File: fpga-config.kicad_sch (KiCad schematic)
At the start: 21 parts, among them J1 PinHeader_2x7_P2mm_SMD_Shroud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, Q1 BSS138PW, Q2 BSS138PW, Q3 BSS138PW, SW1 CVS-03B, SW2 SW_KMR211NGLFS_SMD, U2 TPD4E05U06QDQARQ1, U4 XC7K160T-FFG676

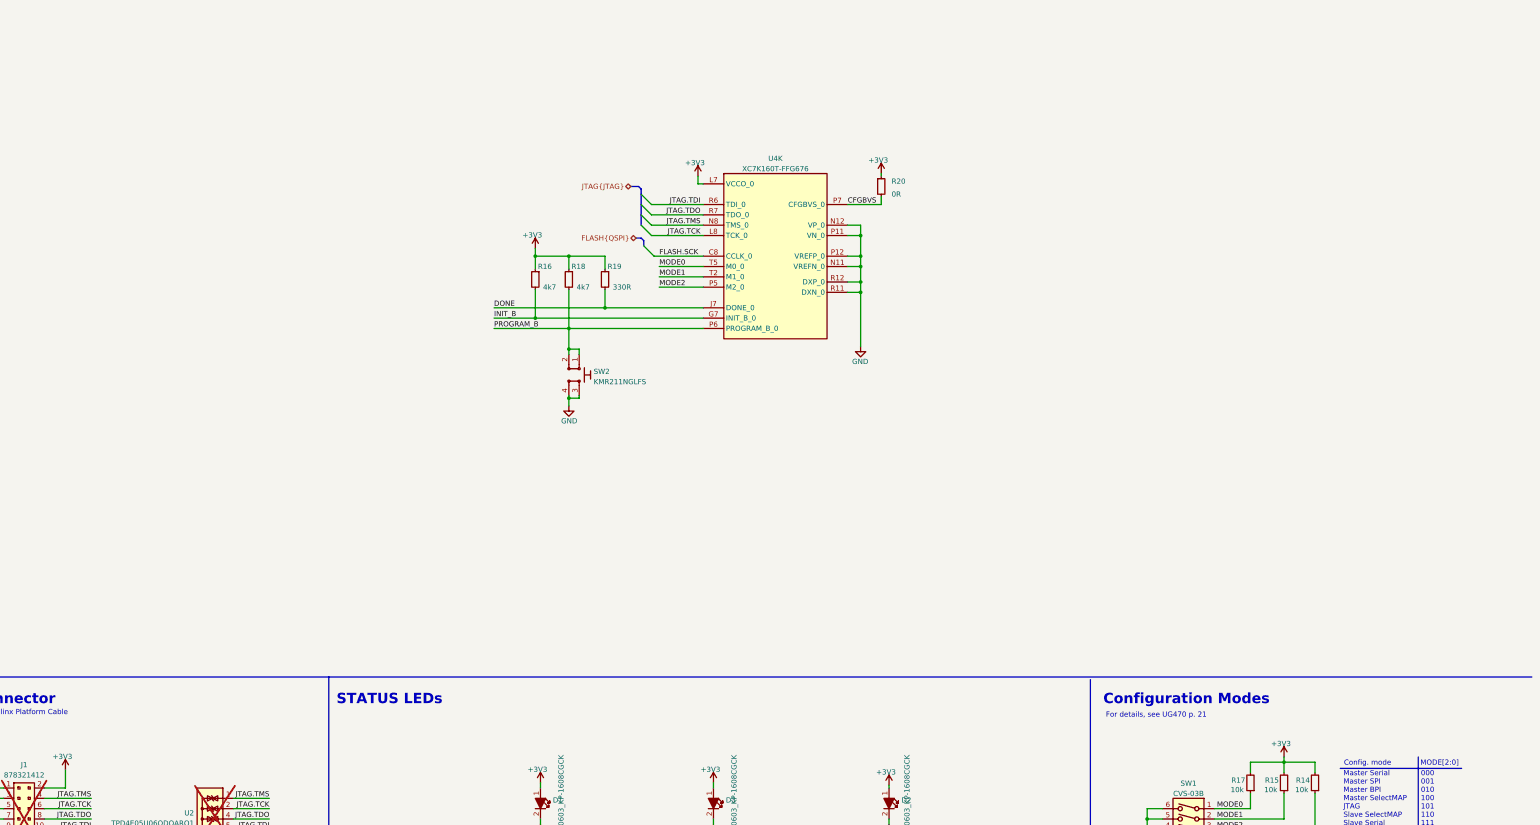
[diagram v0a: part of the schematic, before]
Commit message: [#66311] Add XCAU25P. Reconnect configuration bank 0
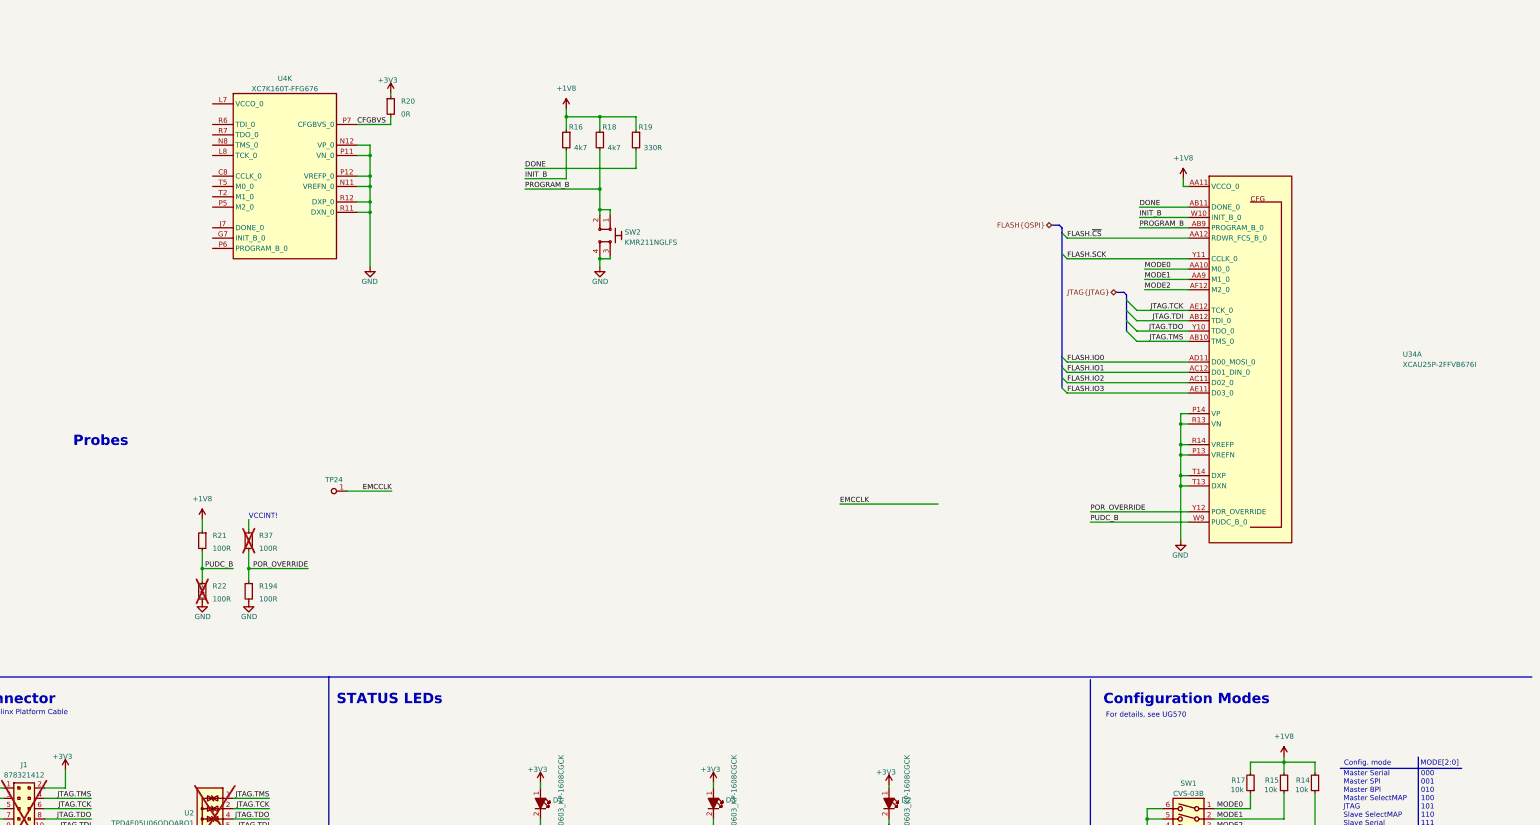
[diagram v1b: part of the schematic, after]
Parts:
- added R194, R21, R22, R37: R_100R_0402, antmicro-footprints:R_0402_1005Metric, symbol antmicroResistors0402:R_100R_0402
- added TP24: TP_1mm_SMD, antmicro-footprints:TP_SMD_1mm, symbol antmicroTestPoints:TP_1mm_SMD
- added U34: XCAU25P-2FFVB676I, antmicro-footprints:BGA-676_27x27mm_Layout26x26_P1x1mm_FFVB676, symbol antmicroFPGAChips:XCAU25P-2FFVB676I
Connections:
- net +3V3: no longer R14.2, R15.2, R16.1, R17.2, R18.1, R19.1, U4.L7 (VCCO_0), U4.T6 (VCCO_0)
- net DONE: now also U34.AB11 (DONE_0); no longer U4.J7 (DONE_0)
- net FLASH.SCK: now also U34.Y11 (CCLK_0); no longer U4.C8 (CCLK_0)
- net GND: now also R194.2, R22.2, U34.P13 (VREFN), U34.P14 (VP), U34.R13 (VN), U34.R14 (VREFP), U34.T13 (DXN), U34.T14 (DXP)
- net INIT_B: now also U34.W10 (INIT_B_0); no longer U4.G7 (INIT_B_0)
- net JTAG.TCK: now also U34.AE12 (TCK_0); no longer U4.L8 (TCK_0)
- net JTAG.TDI: now also U34.AB12 (TDI_0); no longer U4.R6 (TDI_0)
- net JTAG.TDO: now also U34.Y10 (TDO_0); no longer U4.R7 (TDO_0)
- net JTAG.TMS: now also U34.AB10 (TMS_0); no longer U4.N8 (TMS_0)
- net MODE0: now also U34.AA10 (M0_0); no longer U4.T5 (M0_0)
- net MODE1: now also U34.AA9 (M1_0); no longer U4.T2 (M1_0)
- net MODE2: now also U34.AF12 (M2_0); no longer U4.P5 (M2_0)
- net PROGRAM_B: now also U34.AB9 (PROGRAM_B_0); no longer U4.P6 (PROGRAM_B_0)
- new net: U4.L7 (VCCO_0), U4.T6 (VCCO_0)
- new net +1V8: R14.2, R15.2, R16.1, R17.2, R18.1, R19.1, R21.1, U34.AA11 (VCCO_0), U34.AD12 (VCCO_0)
- new net EMCCLK: TP24.1
- new net FLASH.IO0: U34.AD11 (D00_MOSI_0)
- new net FLASH.IO1: U34.AC12 (D01_DIN_0)
- new net FLASH.IO2: U34.AC11 (D02_0)
- new net FLASH.IO3: U34.AE11 (D03_0)
- new net FLASH.~{CS}: U34.AA12 (RDWR_FCS_B_0)
- new net POR_OVERRIDE: R194.1, R37.2, U34.Y12 (POR_OVERRIDE)
- new net PUDC_B: R21.2, R22.1, U34.W9 (PUDC_B_0)
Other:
- note added: "For details, see UG570"
- note added: "Probes"
- note added: "VCCINT!"
- note removed: "For details, see UG470 p. 21"
- moved on the sheet: R16, R18, R19, R20, SW2, U4K

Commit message: [#65754] Rename project
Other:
- title: SO-DIMM DDR5 Tester -> RDIMM DDR5 Tester

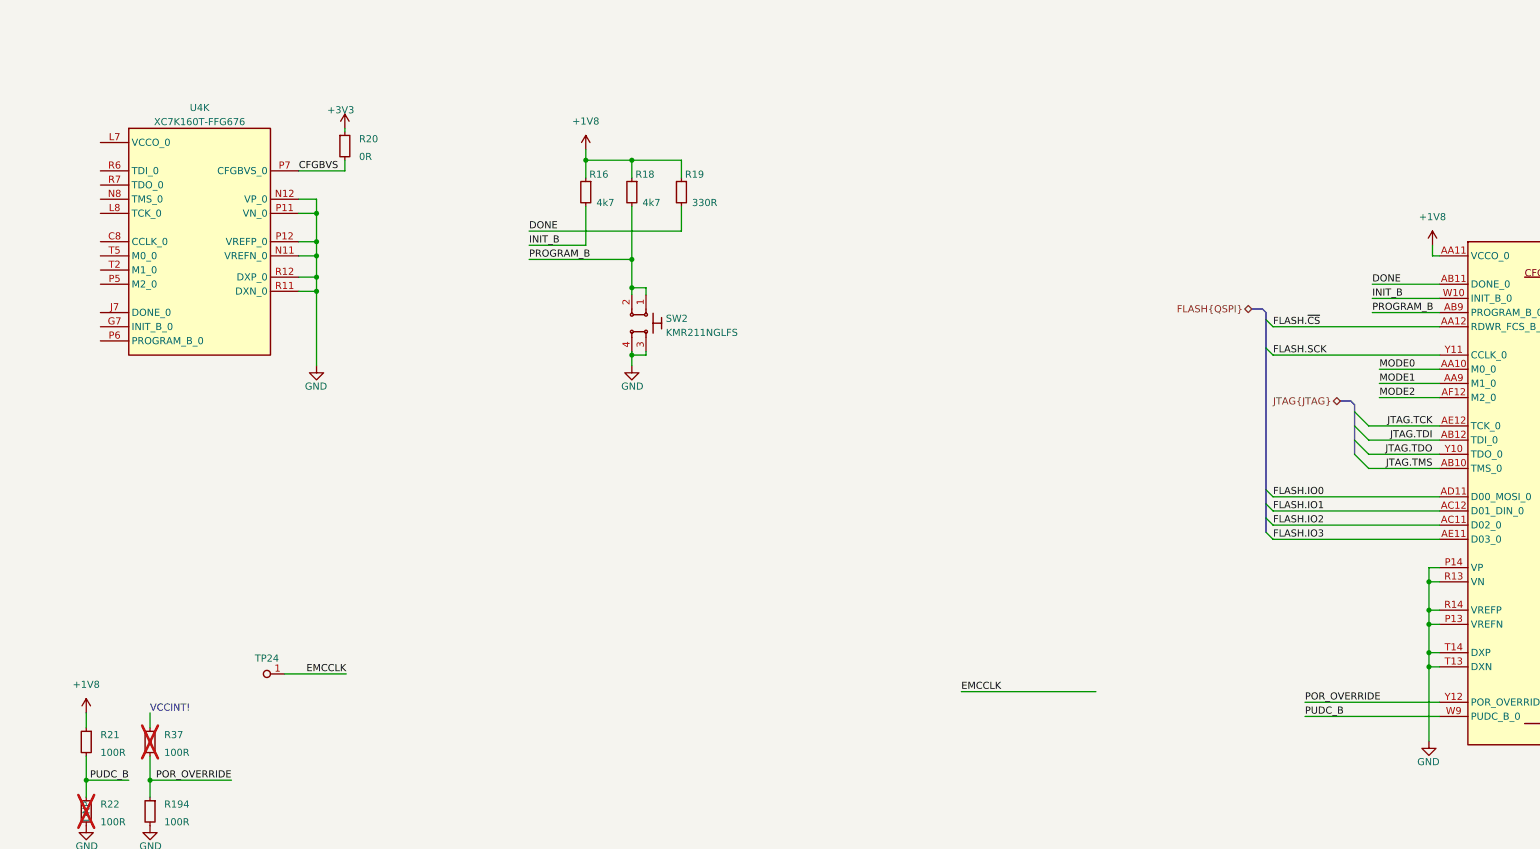
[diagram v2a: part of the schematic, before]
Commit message: [#66311] Add TMP451 remote temperature sensor
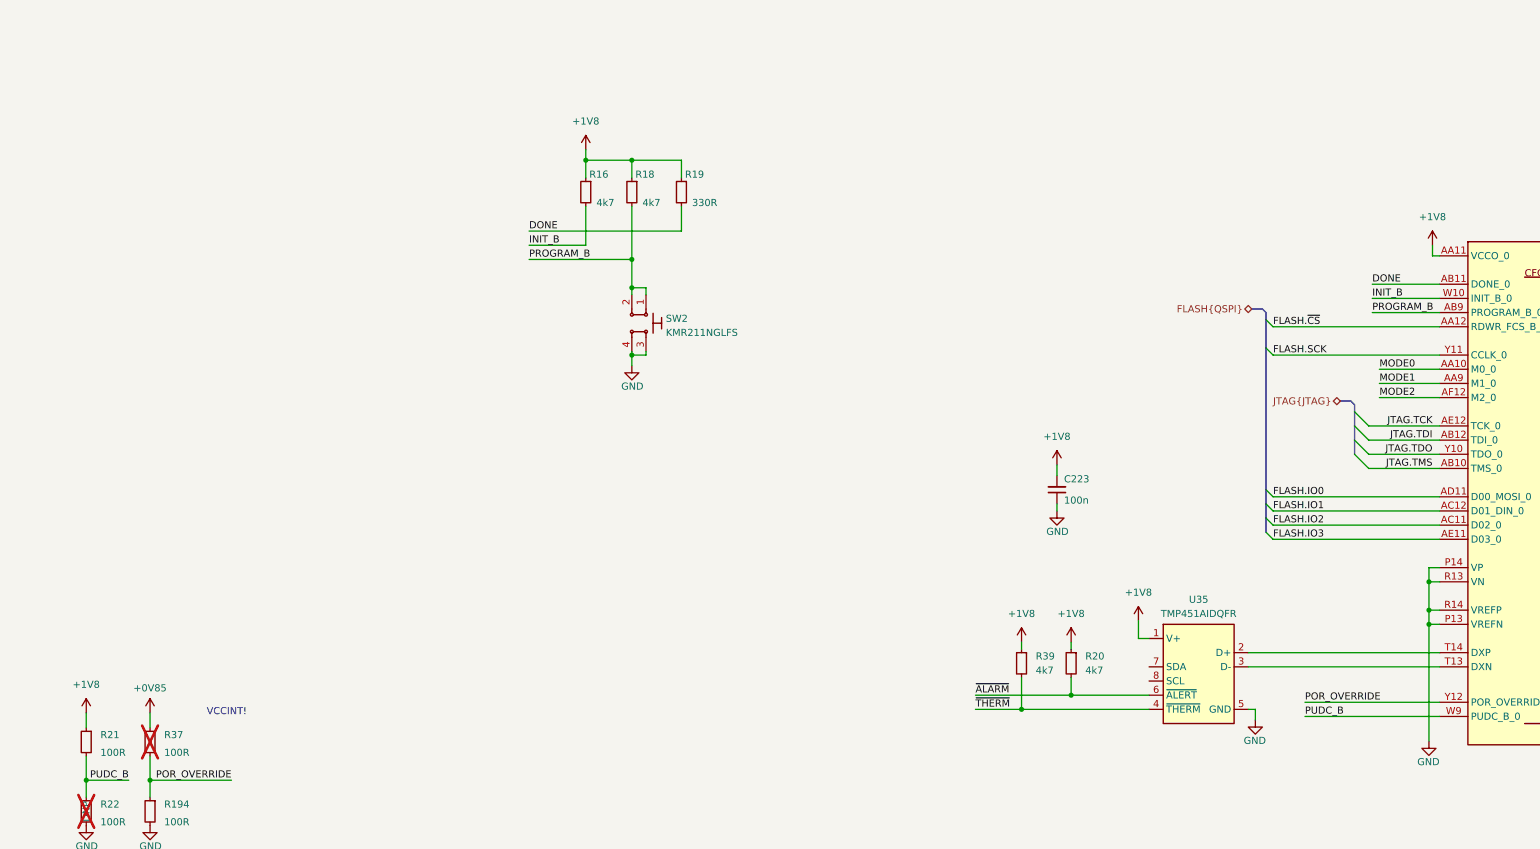
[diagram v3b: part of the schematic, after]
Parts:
- removed R20: R_0R_0402, antmicro-footprints:R_0402_1005Metric, symbol antmicroResistors0402:R_0R_0402
- removed TP24: TP_1mm_SMD, antmicro-footprints:TP_SMD_1mm, symbol antmicroTestPoints:TP_1mm_SMD
- removed U4: XC7K160T-FFG676, antmicro-footprints:BGA-676_27x27mm_Layout26x26_P1x1mm_FFG676, symbol antmicroFPGAChips:XC7K160T-FFG676
- added C223: C_100n_0402, antmicro-footprints:C_0402_1005Metric, symbol antmicroCapacitors0402:C_100n_0402
- added R20, R39: R_4k7_0402, antmicro-footprints:R_0402_1005Metric, symbol antmicroResistors0402:R_4k7_0402
- added U35: TMP451AIDQFR, antmicro-footprints:WSON-8_2x2mm, symbol antmicroTemperatureSensorsAnalogandDigitalOutput:TMP451AIDQFR
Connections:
- net +1V8: now also C223.2, R20.1, R39.1, U35.1 (V+)
- net GND: now also C223.1, U35.5 (GND); no longer U34.T13 (DXN), U34.T14 (DXP)
- net +0V85: now reaches R37.1
- new net: U34.T14 (DXP), U35.2 (D+)
- new net: U34.T13 (DXN), U35.3 (D-)
- new net ~{ALARM}: R20.2, U35.6 (~{ALERT})
- new net ~{THERM}: R39.2, U35.4 (~{THERM})

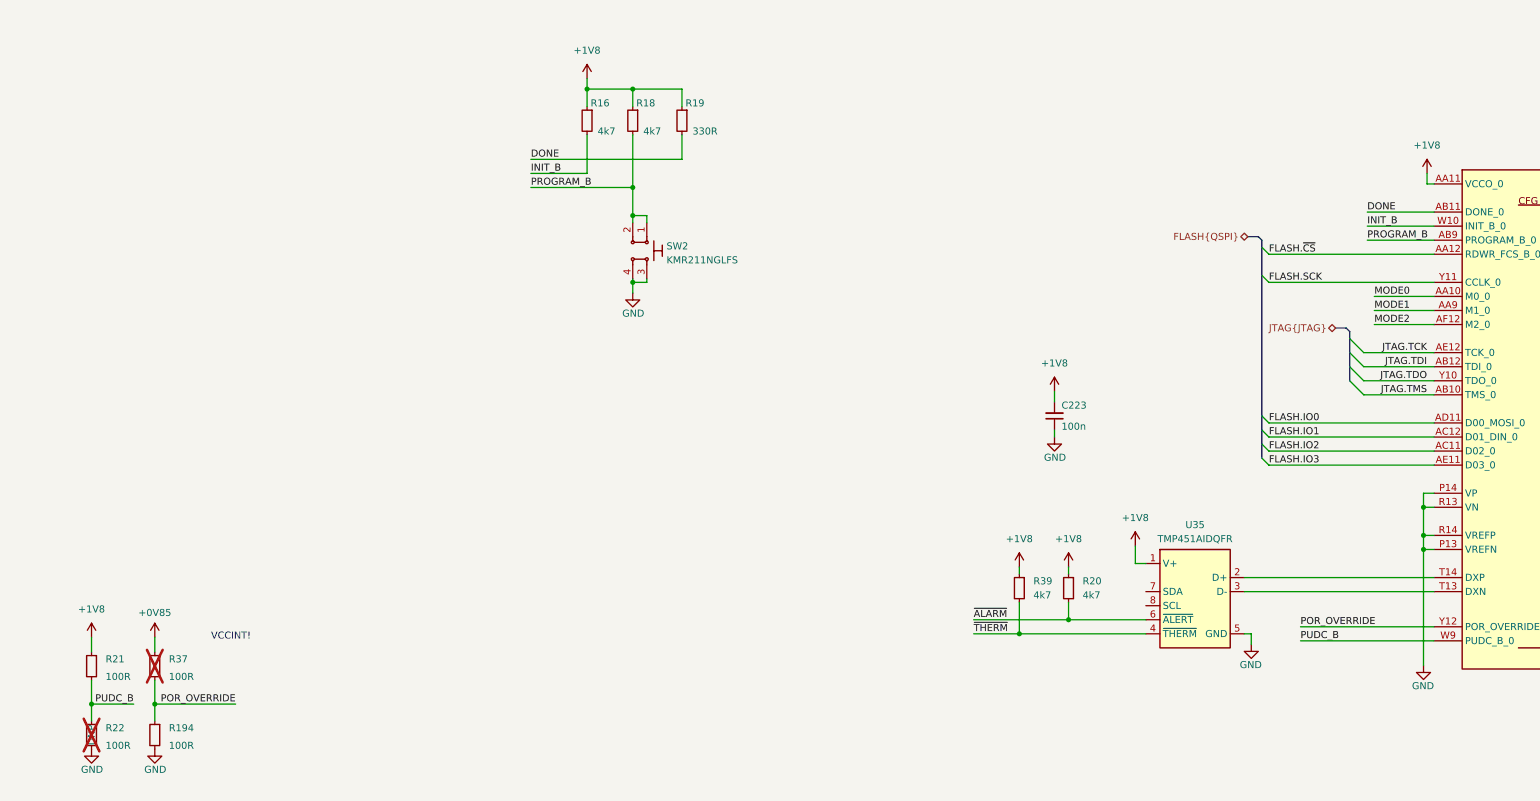
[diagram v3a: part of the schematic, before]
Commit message: [#66311] Replace HyperRam and Flash with 1V8 parts. Add 1V25 ADC VREF for core temp measurement (internal)
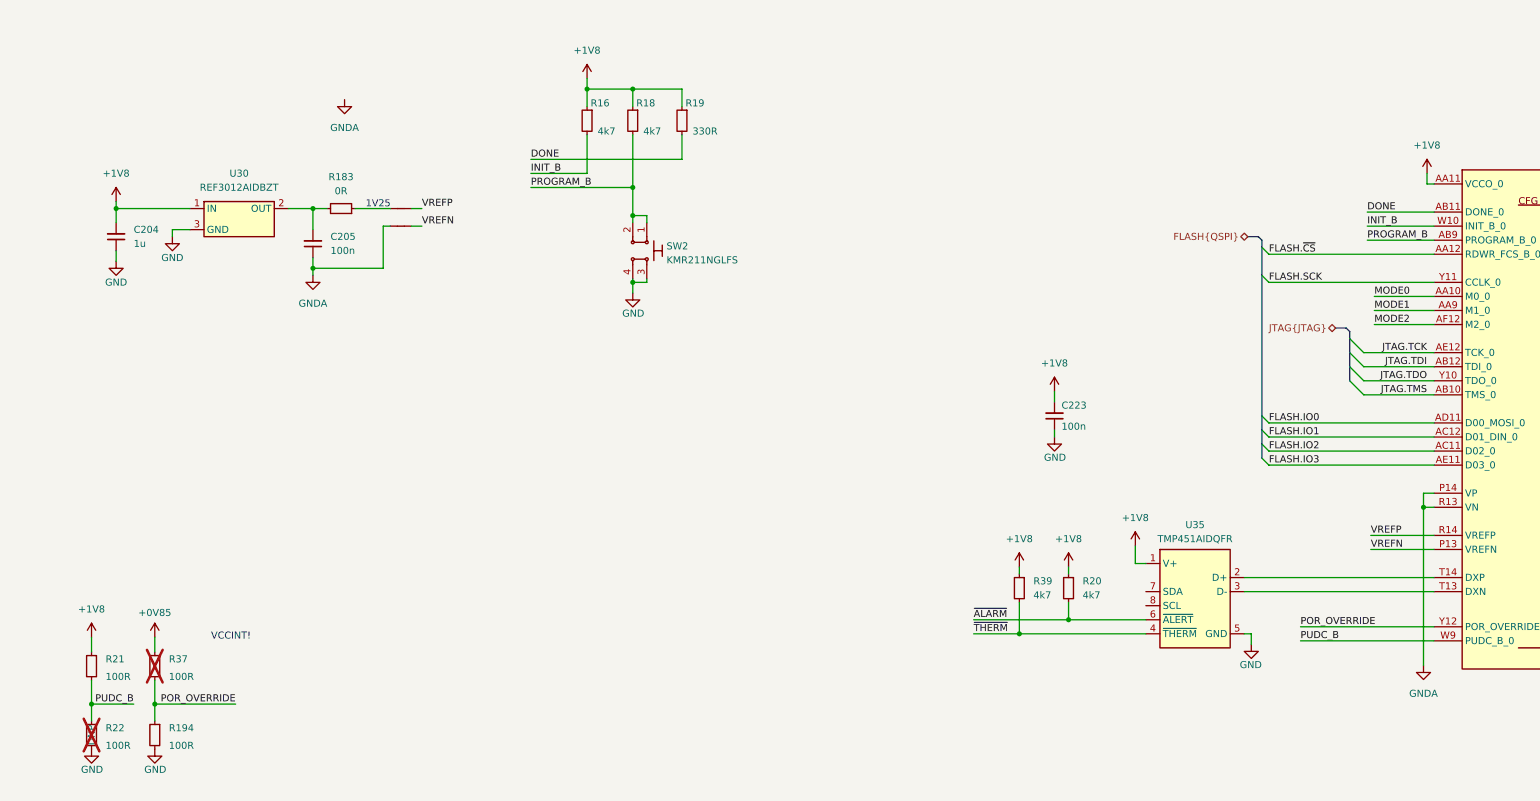
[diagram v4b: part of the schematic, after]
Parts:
- added C204: C_1u_0402, antmicro-footprints:C_0402_1005Metric, symbol antmicroCapacitors0402:C_1u_0402
- added C205: C_100n_0402, antmicro-footprints:C_0402_1005Metric, symbol antmicroCapacitors0402:C_100n_0402
- added NT17, NT18: Net-Tie_2, K410T-devboard-footprints:NetTie-2_SMD_Pad0.127mm, symbol K410T-devboard:Net-Tie_2
- added R183: R_0R_0402, antmicro-footprints:R_0402_1005Metric, symbol antmicroResistors0402:R_0R_0402
- added U30: REF3012AIDBZT, antmicro-footprints:SOT-23-3, symbol antmicroPMICPowerDistributionSwitchesLoadDrivers:REF3012AIDBZT
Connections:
- net +1V8: now also C204.2, U30.1 (IN)
- net GND: now also C204.1, U30.3 (GND); no longer U34.P13 (VREFN), U34.P14 (VP), U34.R13 (VN), U34.R14 (VREFP)
- new net: NT17.1, R183.1
- new net: C205.2, R183.2, U30.2 (OUT)
- new net GNDA: C205.1, NT18.1, U34.P14 (VP), U34.R13 (VN)
- new net VREFN: NT18.2, U34.P13 (VREFN)
- new net VREFP: NT17.2, U34.R14 (VREFP)
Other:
- note added: "1V25"
